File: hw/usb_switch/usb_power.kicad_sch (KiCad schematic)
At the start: 12 parts, among them U4 AP22804AW5, U5 NX20P5090

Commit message: Updating footprints
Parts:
- C12, C13, C14: footprint (none) -> Capacitor_SMD:C_0402_1005Metric
- C15: footprint (none) -> Capacitor_SMD:C_0805_2012Metric
- D1: footprint (none) -> alvarop:CD123-B140LR
- R21, R22, R23, R24, R25: footprint (none) -> Resistor_SMD:R_0402_1005Metric
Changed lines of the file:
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@@
 (kicad_sch (version 20210621) (generator eeschema)
   (paper "A4")
+  (junction (at 121.92 53.34) (diameter 0) (color 0 0 0 0))
+  (junction (at 172.72 93.98) (diameter 0) (color 0 0 0 0))
+  (junction (at 177.8 93.98) (diameter 0) (color 0 0 0 0))
+  (junction (at 109.22 88.9) (diameter 0) (color 0 0 0 0))
+  (junction (at 165.1 93.98) (diameter 0) (color 0 0 0 0))
   (junction (at 111.76 35.56) (diameter 0) (color 0 0 0 0))
   (junction (at 86.36 101.6) (diameter 0) (color 0 0 0 0))
-  (junction (at 172.72 93.98) (diameter 0) (color 0 0 0 0))
-  (junction (at 109.22 88.9) (diameter 0) (color 0 0 0 0))
-  (junction (at 121.92 53.34) (diameter 0) (color 0 0 0 0))
-  (junction (at 177.8 93.98) (diameter 0) (color 0 0 0 0))
   (junction (at 86.36 88.9) (diameter 0) (color 0 0 0 0))
-  (junction (at 165.1 93.98) (diameter 0) (color 0 0 0 0))
   (no_connect (at 147.32 53.34))
   (wire (pts (xy 121.92 53.34) (xy 121.92 55.88))
@@
   (symbol (lib_id "power:GND") (at 86.36 111.76 0) (unit 1)
     (in_bom yes) (on_board yes) (fields_autoplaced)
-    (property "Reference" "#PWR051" (id 0) (at 86.36 118.11 0)
+    (property "Reference" "#PWR054" (id 0) (at 86.36 118.11 0)
       (effects (font (size 1.27 1.27)) hide)
     )
@@
       (effects (font (size 1.27 1.27)) (justify left))
     )
-    (property "Footprint" "" (id 2) (at 109.22 93.98 0)
+    (property "Footprint" "Capacitor_SMD:C_0402_1005Metric" (id 2) (at 109.22 93.98 0)
       (effects (font (size 1.27 1.27)) hide)
     )
@@
       (effects (font (size 1.27 1.27)) (justify left))
     )
-    (property "Footprint" "" (id 2) (at 86.36 106.68 0)
+    (property "Footprint" "Resistor_SMD:R_0402_1005Metric" (id 2) (at 86.36 106.68 0)
       (effects (font (size 1.27 1.27)) hide)
     )
@@
   (symbol (lib_id "power:GND") (at 165.1 104.14 0) (unit 1)
     (in_bom yes) (on_board yes) (fields_autoplaced)
-    (property "Reference" "#PWR059" (id 0) (at 165.1 110.49 0)
+    (property "Reference" "#PWR062" (id 0) (at 165.1 110.49 0)
       (effects (font (size 1.27 1.27)) hide)
     )
@@
       (effects (font (size 1.27 1.27)) (justify left))
     )
-    (property "Footprint" "" (id 2) (at 165.1 99.06 0)
+    (property "Footprint" "Capacitor_SMD:C_0402_1005Metric" (id 2) (at 165.1 99.06 0)
       (effects (font (size 1.27 1.27)) hide)
     )
@@
       (effects (font (size 1.27 1.27)) (justify left))
     )
-    (property "Footprint" "" (id 2) (at 121.92 58.42 0)
+    (property "Footprint" "Resistor_SMD:R_0402_1005Metric" (id 2) (at 121.92 58.42 0)
       (effects (font (size 1.27 1.27)) hide)
     )
@@
   (symbol (lib_id "power:GND") (at 111.76 45.72 0) (unit 1)
     (in_bom yes) (on_board yes) (fields_autoplaced)
-    (property "Reference" "#PWR053" (id 0) (at 111.76 52.07 0)
+    (property "Reference" "#PWR056" (id 0) (at 111.76 52.07 0)
       (effects (font (size 1.27 1.27)) hide)
     )
@@
   (symbol (lib_id "power:GND") (at 172.72 104.14 0) (unit 1)
     (in_bom yes) (on_board yes) (fields_autoplaced)
-    (property "Reference" "#PWR060" (id 0) (at 172.72 110.49 0)
+    (property "Reference" "#PWR063" (id 0) (at 172.72 110.49 0)
       (effects (font (size 1.27 1.27)) hide)
     )
@@
   (symbol (lib_id "power:GND") (at 137.16 60.96 0) (unit 1)
     (in_bom yes) (on_board yes) (fields_autoplaced)
-    (property "Reference" "#PWR056" (id 0) (at 137.16 67.31 0)
+    (property "Reference" "#PWR059" (id 0) (at 137.16 67.31 0)
       (effects (font (size 1.27 1.27)) hide)
     )
@@
   (symbol (lib_id "power:+3V3") (at 157.48 101.6 0) (unit 1)
     (in_bom yes) (on_board yes) (fields_autoplaced)
-    (property "Reference" "#PWR058" (id 0) (at 157.48 105.41 0)
+    (property "Reference" "#PWR061" (id 0) (at 157.48 105.41 0)
       (effects (font (size 1.27 1.27)) hide)
     )
@@
   (symbol (lib_id "power:GND") (at 121.92 63.5 0) (unit 1)
     (in_bom yes) (on_board yes) (fields_autoplaced)
-    (property "Reference" "#PWR054" (id 0) (at 121.92 69.85 0)
+    (property "Reference" "#PWR057" (id 0) (at 121.92 69.85 0)
       (effects (font (size 1.27 1.27)) hide)
     )
@@
       (effects (font (size 1.27 1.27)) (justify left))
     )
-    (property "Footprint" "" (id 2) (at 111.76 40.64 0)
+    (property "Footprint" "Capacitor_SMD:C_0402_1005Metric" (id 2) (at 111.76 40.64 0)
       (effects (font (size 1.27 1.27)) hide)
     )
@@
       (effects (font (size 1.27 1.27)) (justify left))
     )
-    (property "Footprint" "" (id 2) (at 127 137.16 0)
+    (property "Footprint" "Resistor_SMD:R_0402_1005Metric" (id 2) (at 127 137.16 0)
       (effects (font (size 1.27 1.27)) hide)
     )
@@
       (effects (font (size 1.27 1.27)) (justify left))
     )
-    (property "Footprint" "" (id 2) (at 86.36 96.52 0)
+    (property "Footprint" "Resistor_SMD:R_0402_1005Metric" (id 2) (at 86.36 96.52 0)
       (effects (font (size 1.27 1.27)) hide)
     )
@@
   (symbol (lib_id "power:GND") (at 139.7 111.76 0) (unit 1)
     (in_bom yes) (on_board yes) (fields_autoplaced)
-    (property "Reference" "#PWR057" (id 0) (at 139.7 118.11 0)
+    (property "Reference" "#PWR060" (id 0) (at 139.7 118.11 0)
       (effects (font (size 1.27 1.27)) hide)
     )
@@
       (effects (font (size 1.27 1.27)) (justify right))
     )
-    (property "Footprint" "" (id 2) (at 177.8 80.01 0)
+    (property "Footprint" "alvarop:CD123-B140LR" (id 2) (at 177.8 80.01 0)
       (effects (font (size 1.27 1.27)) hide)
     )
@@
       (effects (font (size 1.27 1.27)) (justify left))
     )
-    (property "Footprint" "" (id 2) (at 172.72 99.06 0)
+    (property "Footprint" "Capacitor_SMD:C_0805_2012Metric" (id 2) (at 172.72 99.06 0)
       (effects (font (size 1.27 1.27)) hide)
     )
@@
       (effects (font (size 1.27 1.27)) (justify left))
     )
-    (property "Footprint" "" (id 2) (at 157.48 106.68 0)
+    (property "Footprint" "Resistor_SMD:R_0402_1005Metric" (id 2) (at 157.48 106.68 0)
       (effects (font (size 1.27 1.27)) hide)
     )
@@
   (symbol (lib_id "power:+3V3") (at 127 132.08 0) (unit 1)
     (in_bom yes) (on_board yes) (fields_autoplaced)
-    (property "Reference" "#PWR055" (id 0) (at 127 135.89 0)
+    (property "Reference" "#PWR058" (id 0) (at 127 135.89 0)
       (effects (font (size 1.27 1.27)) hide)
     )
@@
   (symbol (lib_id "power:GND") (at 109.22 99.06 0) (unit 1)
     (in_bom yes) (on_board yes)
-    (property "Reference" "#PWR052" (id 0) (at 109.22 105.41 0)
-      (effects (font (size 1.27 1.27)) hide)
-    )
+    (property "Reference" "#PWR055" (id 0) (at 109.22 105.41 0)
+      (effects (font (size 1.27 1.27)) hide)
+    )

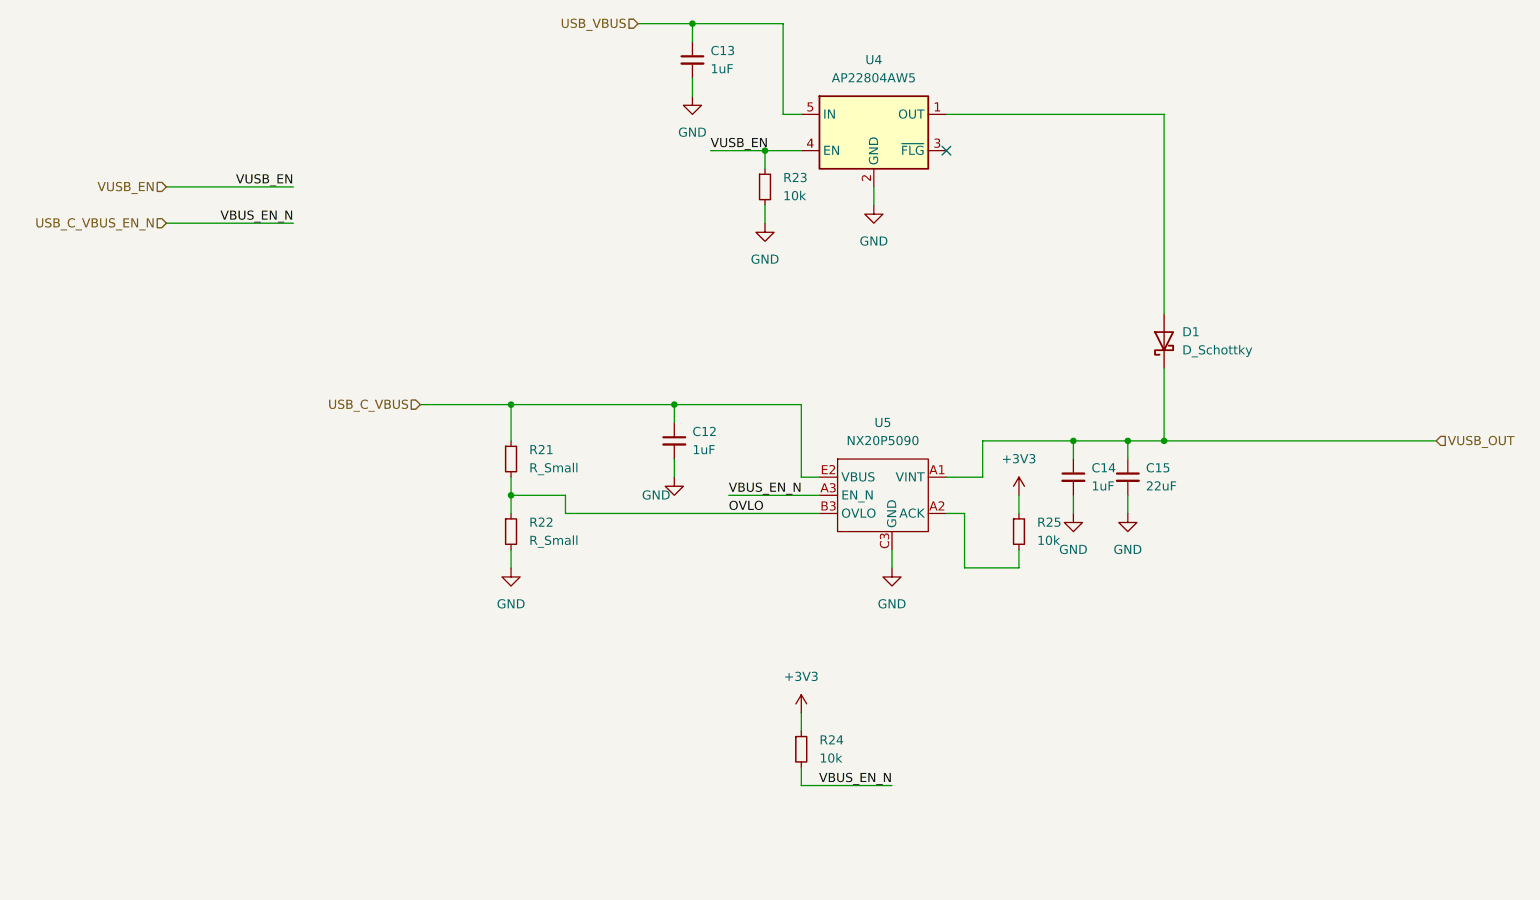
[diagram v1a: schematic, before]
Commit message: Some part changes and started layout
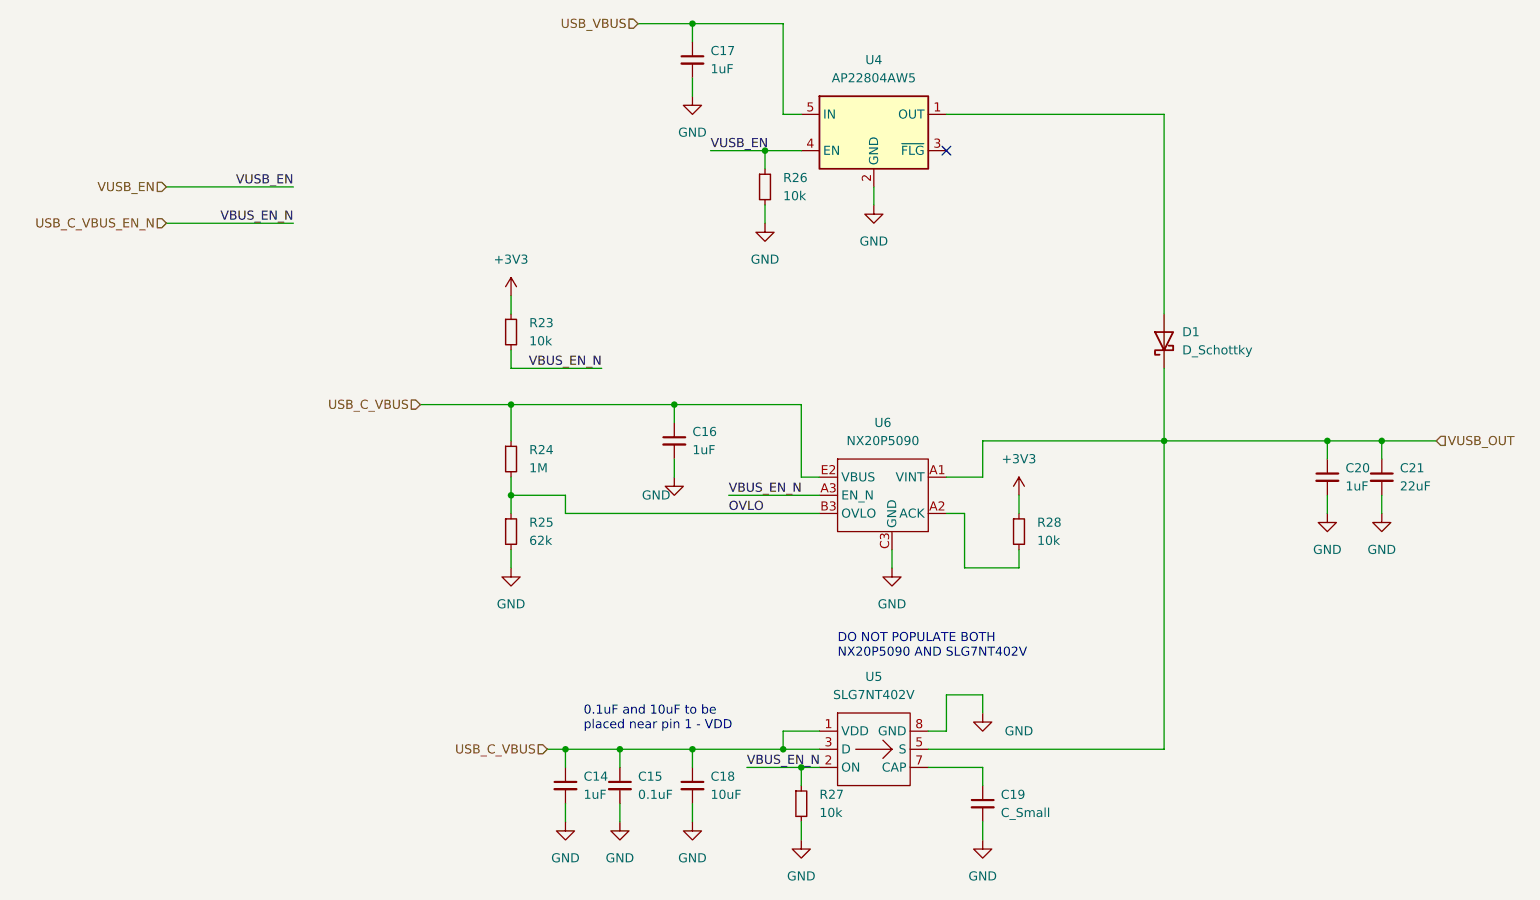
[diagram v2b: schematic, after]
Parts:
- added C14: 1uF, Capacitor_SMD:C_0402_1005Metric, symbol Device:C_Small
- added C15: 0.1uF, Capacitor_SMD:C_0402_1005Metric, symbol Device:C_Small
- added C18: 10uF, Capacitor_SMD:C_0603_1608Metric, symbol Device:C_Small
- added C19: C_Small, Capacitor_SMD:C_0402_1005Metric, symbol Device:C_Small
- added R27: 10k, Resistor_SMD:R_0402_1005Metric, symbol Device:R_Small
- added U5: SLG7NT402V, alvarop:FC-TDFN-8, symbol quesadillon:SLG7NT402V
- R24: renamed from R21; value R_Small -> 1M
- R25: renamed from R22; value R_Small -> 62k
- U6: renamed from U5; footprint (none) -> alvarop:NX20P5090UK
- renumbered C12 to C16, C13 to C17, C14 to C20, C15 to C21, R24 to R23, R23 to R26, R25 to R28
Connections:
- net GND: now also C14.2, C15.2, C18.2, C19.2, R27.2, U5.8 (GND)
- net USB_C_VBUS_EN_N: now also R27.1, U5.2 (ON)
- net VBUS: now also C14.1, C15.1, C18.1, U5.1 (VDD), U5.3 (D)
- net VUSB_OUT: now also U5.5 (S)
- new net: C19.1, U5.7 (CAP)
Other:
- note added: "0.1uF and 10uF to be placed near pin 1 - VDD"
- note added: "DO NOT POPULATE BOTH NX20P5090 AND SLG7NT402V"
- company: (none) -> Quesadillon LLC
- title: (none) -> Debugotron - USB Switch
- moved on the sheet: C20, C21, R23

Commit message: Added MPNs and values to usb_switch
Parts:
- C14, C17: value 1uF -> 1uF 16V
- C16, C20: value 1uF -> 1uF 35V
- C18: value 10uF -> 10uF 10V
- C19: value C_Small -> 0.01uF
- C21: value 22uF -> 22uF 25V
- D1: MPN (none) -> CD123D-B140LR
- U4: MPN (none) -> AP22804AW5-7
- U5: MPN (none) -> SLG7NT402V
- U6: MPN (none) -> NX20P5090UKAZ
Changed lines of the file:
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@@
       (effects (font (size 1.27 1.27)) (justify left))
     )
-    (property "Value" "C_Small" (id 1) (at 154.94 146.0562 0)
+    (property "Value" "0.01uF" (id 1) (at 154.94 146.0562 0)
       (effects (font (size 1.27 1.27)) (justify left))
     )
@@
       (effects (font (size 1.27 1.27)) hide)
     )
+    (property "MPN" "AP22804AW5-7" (id 4) (at 137.16 50.8 0)
+      (effects (font (size 1.27 1.27)) hide)
+    )
     (pin "1")
     (pin "2")
@@
       (effects (font (size 1.27 1.27)) (justify left))
     )
-    (property "Value" "1uF" (id 1) (at 111.76 95.2499 0)
+    (property "Value" "1uF 35V" (id 1) (at 111.76 95.2499 0)
       (effects (font (size 1.27 1.27)) (justify left))
     )
@@
       (effects (font (size 1.27 1.27)) (justify left))
     )
-    (property "Value" "10uF" (id 1) (at 114.3 143.5162 0)
+    (property "Value" "10uF 10V" (id 1) (at 114.3 143.5162 0)
       (effects (font (size 1.27 1.27)) (justify left))
     )
@@
   )
   (symbol (lib_id "Device:C_Small") (at 200.66 99.06 0) (unit 1)
-    (in_bom yes) (on_board yes) (fields_autoplaced)
-    (property "Reference" "C20" (id 0) (at 203.2 97.7899 0)
-      (effects (font (size 1.27 1.27)) (justify left))
-    )
-    (property "Value" "1uF" (id 1) (at 203.2 100.3299 0)
+    (in_bom yes) (on_board yes)
+    (property "Reference" "C20" (id 0) (at 193.04 99.06 0)
+      (effects (font (size 1.27 1.27)) (justify left))
+    )
+    (property "Value" "1uF 35V" (id 1) (at 190.5 101.6 0)
       (effects (font (size 1.27 1.27)) (justify left))
     )
@@
   )
   (symbol (lib_id "Device:C_Small") (at 93.98 142.24 0) (unit 1)
-    (in_bom yes) (on_board yes) (fields_autoplaced)
-    (property "Reference" "C14" (id 0) (at 96.52 140.9699 0)
-      (effects (font (size 1.27 1.27)) (justify left))
-    )
-    (property "Value" "1uF" (id 1) (at 96.52 143.5099 0)
+    (in_bom yes) (on_board yes)
+    (property "Reference" "C14" (id 0) (at 86.36 142.24 0)
+      (effects (font (size 1.27 1.27)) (justify left))
+    )
+    (property "Value" "1uF 16V" (id 1) (at 83.82 144.78 0)
       (effects (font (size 1.27 1.27)) (justify left))
     )
@@
   (symbol (lib_id "Device:C_Small") (at 111.76 40.64 0) (unit 1)
     (in_bom yes) (on_board yes) (fields_autoplaced)
-    (property "Reference" "C17" (id 0) (at 114.3 39.3699 0)
-      (effects (font (size 1.27 1.27)) (justify left))
-    )
-    (property "Value" "1uF" (id 1) (at 114.3 41.9099 0)
+    (property "Reference" "C17" (id 0) (at 114.3 39.3762 0)
+      (effects (font (size 1.27 1.27)) (justify left))
+    )
+    (property "Value" "1uF 16V" (id 1) (at 114.3 41.9162 0)
       (effects (font (size 1.27 1.27)) (justify left))
     )
@@
     )
     (property "Datasheet" "" (id 3) (at 139.7 96.52 0)
+      (effects (font (size 1.27 1.27)) hide)
+    )
+    (property "MPN" "NX20P5090UKAZ" (id 4) (at 139.7 101.6 0)
       (effects (font (size 1.27 1.27)) hide)
     )
@@
       (effects (font (size 1.27 1.27)) hide)
     )
+    (property "MPN" "CD123D-B140LR" (id 4) (at 177.8 80.01 0)
+      (effects (font (size 1.27 1.27)) hide)
+    )
     (pin "1")
     (pin "2")
@@
   (symbol (lib_id "Device:C_Small") (at 208.28 99.06 0) (unit 1)
     (in_bom yes) (on_board yes) (fields_autoplaced)
-    (property "Reference" "C21" (id 0) (at 210.82 97.7899 0)
-      (effects (font (size 1.27 1.27)) (justify left))
-    )
-    (property "Value" "22uF" (id 1) (at 210.82 100.3299 0)
+    (property "Reference" "C21" (id 0) (at 210.82 97.7962 0)
+      (effects (font (size 1.27 1.27)) (justify left))
+    )
+    (property "Value" "22uF 25V" (id 1) (at 210.82 100.3362 0)
       (effects (font (size 1.27 1.27)) (justify left))
     )
@@
       (effects (font (size 1.27 1.27)) hide)
     )
+    (property "MPN" "SLG7NT402V" (id 4) (at 137.16 137.16 0)
+      (effects (font (size 1.27 1.27)) hide)
+    )
